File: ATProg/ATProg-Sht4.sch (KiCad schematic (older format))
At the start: 3 parts, among them U3 ATMEGA328-PU, Y2 16MHz

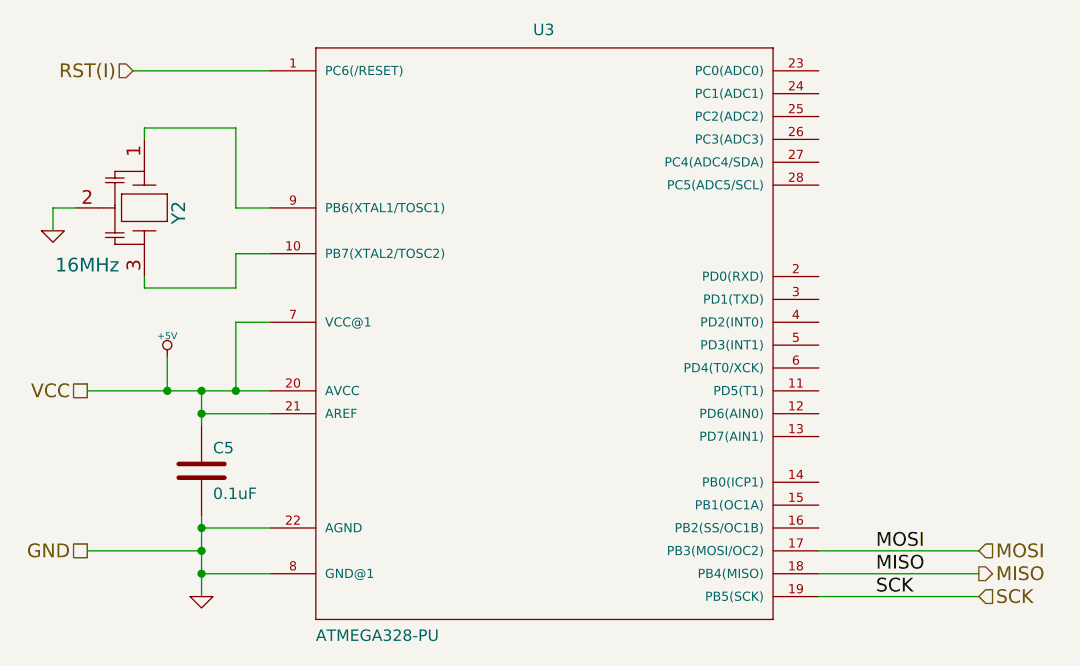
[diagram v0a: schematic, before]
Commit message: Worked ATMega Programmer design
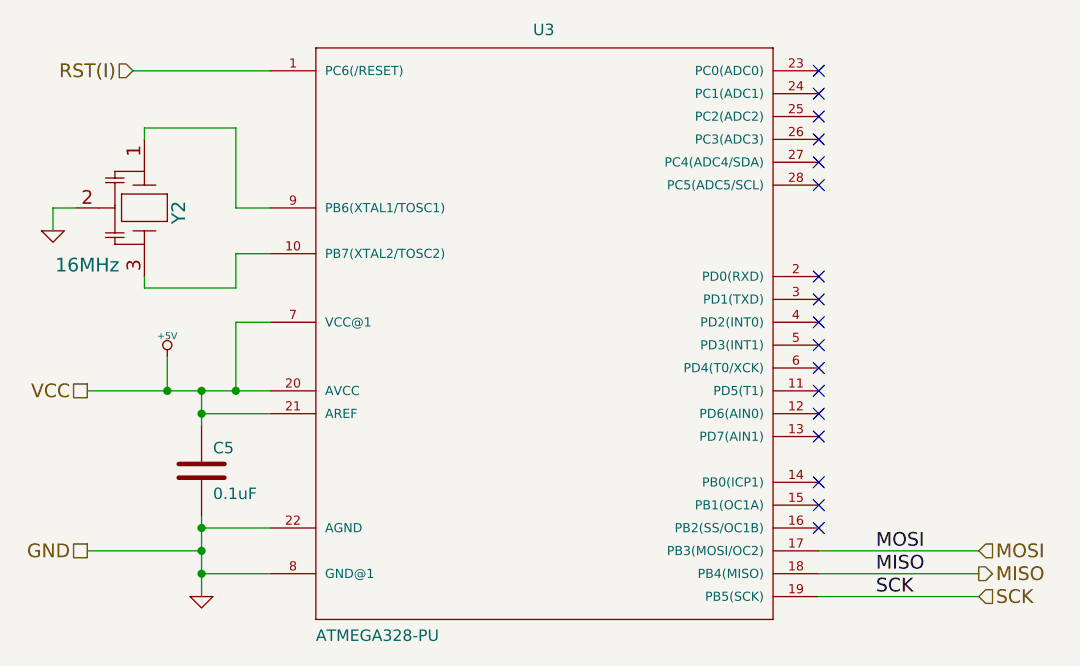
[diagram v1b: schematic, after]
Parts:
- U3: footprint DIP-28__300 -> TEXTOOL-28N
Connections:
- no-connect marks 0 -> 17
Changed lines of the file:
@@
-EESchema Schematic File Version 2  date 17/09/2013 16:26:56
+EESchema Schematic File Version 2  date 18/09/2013 15:19:46
 LIBS:DougsSch
 LIBS:resonator_3pins
@@
 $Descr A 11000 8500
 encoding utf-8
-Sheet 4 5
+Sheet 4 6
 Title "MiniDuino"
-Date "17 sep 2013"
+Date "18 sep 2013"
 Rev "X2"
 Comp ""
@@
 F 0 "U3" H 5650 5000 50  0000 L BNN
 F 1 "ATMEGA328-PU" H 4700 2350 50  0000 L BNN
-F 2 "DIP-28__300" H 5700 3900 50  0001 C CNN
+F 2 "TEXTOOL-28N" H 5700 3900 50  0001 C CNN
 F 3 "" H 5700 3750 60  0001 C CNN
 	1    5700 3750
@@
 Text HLabel 7600 4950 2    60   Input ~ 0
 SCK
+NoConn ~ 6900 2650
+NoConn ~ 6900 2750
+NoConn ~ 6900 2850
+NoConn ~ 6900 2950
+NoConn ~ 6900 3050
+NoConn ~ 6900 3150
+NoConn ~ 6900 3550
+NoConn ~ 6900 3650
+NoConn ~ 6900 3750
+NoConn ~ 6900 3850
+NoConn ~ 6900 3950
+NoConn ~ 6900 4050
+NoConn ~ 6900 4150
+NoConn ~ 6900 4250
+NoConn ~ 6900 4450
+NoConn ~ 6900 4550
+NoConn ~ 6900 4650
 $EndSCHEMATC
